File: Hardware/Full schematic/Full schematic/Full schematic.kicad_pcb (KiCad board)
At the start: 2 copper layers, 111 parts, among them J1 Conn_01x04_Male, J2 Conn_01x04_Male, J3 Conn_01x02_Male, J4 Conn_01x02_Male, J5 Conn_01x02_Male, J6 Conn_01x02_Male, J7 Conn_01x02_Male, J8 Conn_01x06_Male, K1 EDR101A0500, K2 EDR101A0500, K3 EDR101A0500, K4 EDR101A0500, K5 EDR101A0500, Q1 BSS138, Q2 IRF610, Q3 IRLML2502, Q4 IRLML2502, Q5 IRLML2502, Q6 IRLML2502, Q7 IRLML2502, U1 74LVC2T45DC, U2 74LVC2T45DC, U3 AD9835, X1 50MHz

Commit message: After prototype built
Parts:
- C23: value 0.01uF -> 10nF
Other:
- board outline added: 83.6 x 61.5 mm

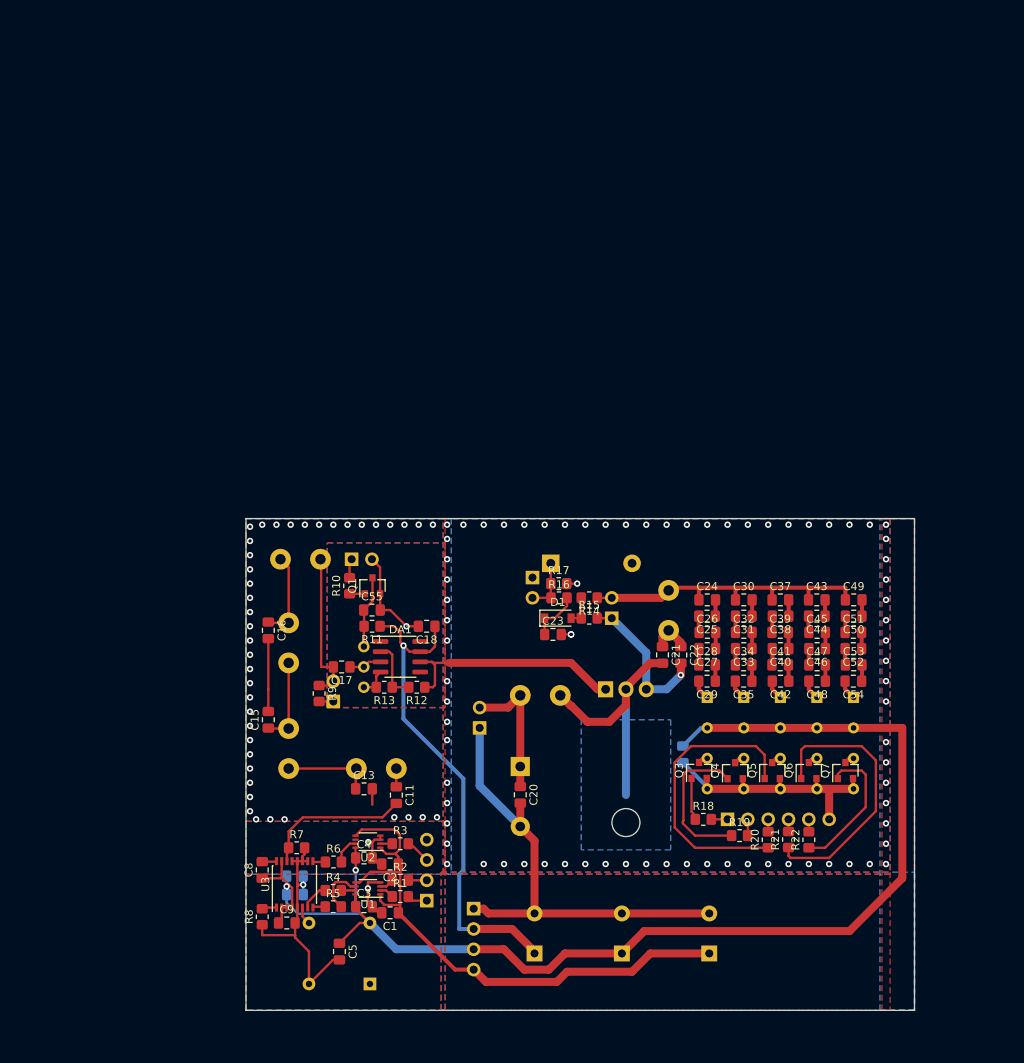
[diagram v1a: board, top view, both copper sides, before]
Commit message: Second prototype PCB is almost ready
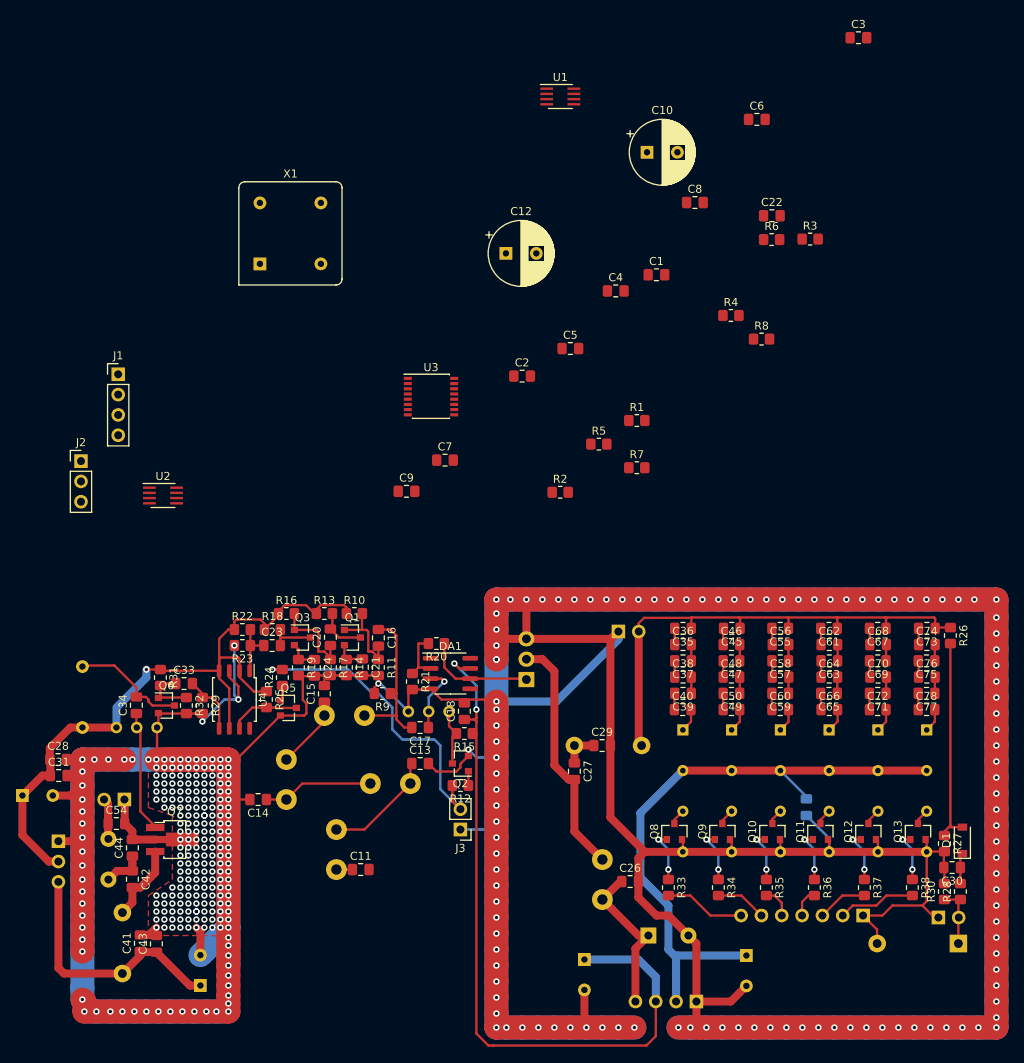
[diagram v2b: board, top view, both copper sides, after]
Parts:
- added C56: 100pF, Capacitor_SMD:C_0805_2012Metric_Pad1.18x1.45mm_HandSolder, F.Cu at (142.8, 103.6)
- added C57: 100pF, Capacitor_SMD:C_0805_2012Metric_Pad1.18x1.45mm_HandSolder, F.Cu at (142.7, 105.7)
- added C58: 100pF, Capacitor_SMD:C_0805_2012Metric_Pad1.18x1.45mm_HandSolder, F.Cu at (142.8, 107.7)
- added C59: 100pF, Capacitor_SMD:C_0805_2012Metric_Pad1.18x1.45mm_HandSolder, F.Cu at (142.7, 109.7)
- added C60: 100pF, Capacitor_SMD:C_0805_2012Metric_Pad1.18x1.45mm_HandSolder, F.Cu at (142.7, 111.8)
- added C61: 47pF, Capacitor_SMD:C_0805_2012Metric_Pad1.18x1.45mm_HandSolder, F.Cu at (148.8, 101.6)
- added C62: 47pF, Capacitor_SMD:C_0805_2012Metric_Pad1.18x1.45mm_HandSolder, F.Cu at (148.9, 103.6)
- added C63: 47pF, Capacitor_SMD:C_0805_2012Metric_Pad1.18x1.45mm_HandSolder, F.Cu at (148.9, 105.7)
- added C64: 47pF, Capacitor_SMD:C_0805_2012Metric_Pad1.18x1.45mm_HandSolder, F.Cu at (148.9, 107.7)
- added C65: 47pF, Capacitor_SMD:C_0805_2012Metric_Pad1.18x1.45mm_HandSolder, F.Cu at (148.8, 109.7)
- added C66: 47pF, Capacitor_SMD:C_0805_2012Metric_Pad1.18x1.45mm_HandSolder, F.Cu at (148.9, 111.8)
- added C67: 24pF, Capacitor_SMD:C_0805_2012Metric_Pad1.18x1.45mm_HandSolder, F.Cu at (154.9, 101.6)
- added C68: 24pF, Capacitor_SMD:C_0805_2012Metric_Pad1.18x1.45mm_HandSolder, F.Cu at (155.0, 103.6)
- added C69: 24pF, Capacitor_SMD:C_0805_2012Metric_Pad1.18x1.45mm_HandSolder, F.Cu at (154.9, 105.7)
- added C70: 24pF, Capacitor_SMD:C_0805_2012Metric_Pad1.18x1.45mm_HandSolder, F.Cu at (155.0, 107.7)
- added C71: 24pF, Capacitor_SMD:C_0805_2012Metric_Pad1.18x1.45mm_HandSolder, F.Cu at (154.9, 109.7)
- added C72: 24pF, Capacitor_SMD:C_0805_2012Metric_Pad1.18x1.45mm_HandSolder, F.Cu at (154.9, 111.8)
- added C73: 12pF, Capacitor_SMD:C_0805_2012Metric_Pad1.18x1.45mm_HandSolder, F.Cu at (161.1, 101.6)
- added C74: 12pF, Capacitor_SMD:C_0805_2012Metric_Pad1.18x1.45mm_HandSolder, F.Cu at (161.1, 103.6)
- added C75: 12pF, Capacitor_SMD:C_0805_2012Metric_Pad1.18x1.45mm_HandSolder, F.Cu at (161.0, 105.7)
- added C76: 12pF, Capacitor_SMD:C_0805_2012Metric_Pad1.18x1.45mm_HandSolder, F.Cu at (161.1, 107.7)
- added C77: 12pF, Capacitor_SMD:C_0805_2012Metric_Pad1.18x1.45mm_HandSolder, F.Cu at (161.0, 109.7)
- added C78: 12pF, Capacitor_SMD:C_0805_2012Metric_Pad1.18x1.45mm_HandSolder, F.Cu at (161.0, 111.8)
- added J9: Conn_01x07_Male, Connector_PinHeader_2.54mm:PinHeader_1x07_P2.54mm_Vertical, B.Cu at (153.1, 137.5)
- added K6: EDR101A0500, Relay_THT:Relay_SPST_StandexMeder_SIL_Form1A, B.Cu at (161.0, 114.3)
- added L7: 200nH, Inductor_THT:L_Axial_L5.3mm_D2.2mm_P7.62mm_Horizontal_Vishay_IM-1, B.Cu at (55.5, 114.0)
- added L8: 300nH, Inductor_THT:L_Axial_L16.0mm_D7.5mm_P7.62mm_Vertical_Fastron_XHBCC, B.Cu at (60.5, 144.8)
- added L9: 23.5nH, Inductor_THT:L_Axial_L9.5mm_D4.0mm_P5.08mm_Vertical_Fastron_SMCC, B.Cu at (58.8, 133.0)
- added Q10: IRLML2502, Package_TO_SOT_SMD:SOT-23, F.Cu at (141.8, 127.0)
- added Q11: IRLML2502, Package_TO_SOT_SMD:SOT-23, F.Cu at (147.8, 127.0)
- added Q12: IRLML2502, Package_TO_SOT_SMD:SOT-23, F.Cu at (153.8, 127.0)
- added Q13: IRLML2502, Package_TO_SOT_SMD:SOT-23, F.Cu at (159.9, 127.0)
- added Q8: IRLML2502, Package_TO_SOT_SMD:SOT-23, F.Cu at (129.5, 127.0)
- added Q9: IRLML2502, Package_TO_SOT_SMD:SOT-23, F.Cu at (135.5, 127.0)
- added R23: 4.7k, Resistor_SMD:R_0805_2012Metric_Pad1.20x1.40mm_HandSolder, F.Cu at (75.5, 103.8)
- added R24: 100, Resistor_SMD:R_0805_2012Metric_Pad1.20x1.40mm_HandSolder, F.Cu at (80.5, 107.8)
- added R25: 47k, Resistor_SMD:R_0805_2012Metric_Pad1.20x1.40mm_HandSolder, F.Cu at (78.5, 110.5)
- added R26: 220k, Resistor_SMD:R_0805_2012Metric_Pad1.20x1.40mm_HandSolder, F.Cu at (164.0, 102.5)
- added R27: 11k, Resistor_SMD:R_0805_2012Metric_Pad1.20x1.40mm_HandSolder, F.Cu at (163.2, 128.5)
- added R28: 39k, Resistor_SMD:R_0805_2012Metric_Pad1.20x1.40mm_HandSolder, F.Cu at (165.2, 134.5)
- added R29: 33, Resistor_SMD:R_0805_2012Metric_Pad1.20x1.40mm_HandSolder, F.Cu at (70.5, 111.2)
- added R30: 10k, Resistor_SMD:R_0805_2012Metric_Pad1.20x1.40mm_HandSolder, F.Cu at (163.2, 134.5)
- added R31: 6.2k, Resistor_SMD:R_0805_2012Metric_Pad1.20x1.40mm_HandSolder, F.Cu at (65.2, 107.8)
- added R32: 1k, Resistor_SMD:R_0805_2012Metric_Pad1.20x1.40mm_HandSolder, F.Cu at (68.5, 111.2)
- added R33: 100, Resistor_SMD:R_0805_2012Metric_Pad1.20x1.40mm_HandSolder, F.Cu at (128.8, 134.0)
- added R34: 100, Resistor_SMD:R_0805_2012Metric_Pad1.20x1.40mm_HandSolder, F.Cu at (135.0, 134.0)
- added R35: 100, Resistor_SMD:R_0805_2012Metric_Pad1.20x1.40mm_HandSolder, F.Cu at (141.0, 134.0)
- added R36: 100, Resistor_SMD:R_0805_2012Metric_Pad1.20x1.40mm_HandSolder, F.Cu at (147.0, 134.0)
- added R37: 100, Resistor_SMD:R_0805_2012Metric_Pad1.20x1.40mm_HandSolder, F.Cu at (153.2, 134.0)
- added R38: 100, Resistor_SMD:R_0805_2012Metric_Pad1.20x1.40mm_HandSolder, F.Cu at (159.2, 134.0)
- added RV2: 20k, Potentiometer_THT:Potentiometer_Bourns_3386C_Horizontal, B.Cu at (59.8, 114.0)
- added U4: ICS501, Package_SO:SOIC-8_5.23x5.23mm_P1.27mm, F.Cu at (74.5, 110.5)
- C10, C12: footprint Capacitor_THT:CP_Radial_D10.0mm_P5.00mm -> Capacitor_THT:CP_Radial_D8.0mm_P3.80mm; moved to F.Cu
- C14: value 470uF x 16V -> 56pF; footprint Capacitor_THT:CP_Radial_D10.0mm_P5.00mm -> Capacitor_SMD:C_0805_2012Metric_Pad1.18x1.45mm_HandSolder; moved to F.Cu
- C15: value 56pF -> 47pF
- C16, C43: value 47pF -> 0.1uF
- C19: value 1000uF x 25V -> 470uFx16V; footprint Capacitor_THT:CP_Radial_D14.0mm_P7.50mm -> Capacitor_THT:CP_Radial_D8.0mm_P3.80mm
- C22: value 75pF -> 10nF
- C23: value 10nF -> 0.1uF
- C24, C26, C27: value 390pF -> 0.1uF
- C25: value 390pF -> 1000uF x 25V; footprint Capacitor_SMD:C_0805_2012Metric_Pad1.18x1.45mm_HandSolder -> Capacitor_THT:CP_Radial_D10.0mm_P5.00mm; moved to B.Cu
- C28: value 390pF -> 1nF
- C29: value 390pF -> 75pF
- C30: value 200pF -> 10nF
- C31: value 200pF -> 0.1uF
- C32: value 200pF -> 470uFx6.3V; footprint Capacitor_SMD:C_0805_2012Metric_Pad1.18x1.45mm_HandSolder -> Capacitor_THT:CP_Radial_D8.0mm_P3.80mm; moved to B.Cu
- C33: value 200pF -> 1nF
- C34: value 200pF -> 75pF
- C35: value 200pF -> 390pF
- C36: value 0.1uF -> 390pF; moved to F.Cu
- C37, C38, C39, C40: value 100pF -> 390pF
- C41, C42: value 100pF -> 1nF
- C44: value 47pF -> 20pF
- C45, C46, C47, C48: value 47pF -> 200pF
- C49, C50: value 24pF -> 200pF
- C51: value 24pF -> 470uF x 10V; footprint Capacitor_SMD:C_0805_2012Metric_Pad1.18x1.45mm_HandSolder -> Capacitor_THT:CP_Radial_D8.0mm_P3.80mm; moved to B.Cu
- C52: value 24pF -> 470uFx6.3V; footprint Capacitor_SMD:C_0805_2012Metric_Pad1.18x1.45mm_HandSolder -> Capacitor_THT:CP_Radial_D8.0mm_P3.80mm; moved to B.Cu
- C53: value 24pF -> 0.1uF; moved to B.Cu
- C54: value 24pF -> 56pF
- C55: value 10nF -> 100pF
- C6, C7, J1, J3, X1: moved to F.Cu
- J2: value Conn_01x04_Male -> Conn_01x03_Male; footprint Connector_PinHeader_2.54mm:PinHeader_1x04_P2.54mm_Vertical -> Connector_PinHeader_2.54mm:PinHeader_1x03_P2.54mm_Vertical; moved to F.Cu
- J4: value Conn_01x02_Male -> Conn_01x04_Male; footprint Connector_PinHeader_2.54mm:PinHeader_1x02_P2.54mm_Vertical -> Connector_PinHeader_2.54mm:PinHeader_1x04_P2.54mm_Vertical
- J5: value Conn_01x02_Male -> Conn_01x03_Male; footprint Connector_PinHeader_2.54mm:PinHeader_1x02_P2.54mm_Vertical -> Connector_PinHeader_2.54mm:PinHeader_1x03_P2.54mm_Vertical
- J8: value Conn_01x06_Male -> Conn_01x02_Male; footprint Connector_PinHeader_2.54mm:PinHeader_1x06_P2.54mm_Vertical -> Connector_PinHeader_2.54mm:PinHeader_1x02_P2.54mm_Vertical
- K1, K2, K3, K4, K5: footprint Relay_THT:Relay_SPST_StandexMeder_MS_Form1AB -> Relay_THT:Relay_SPST_StandexMeder_SIL_Form1A
- L6: footprint Inductor_THT:L_Radial_D9.5mm_P5.00mm_Fastron_07HVP -> Inductor_THT:L_Toroid_Vertical_L21.6mm_W9.1mm_P8.40mm_Bourns_5700
- Q1: value BSS138 -> BC847
- Q2: value IRF610 -> BSS138; footprint Package_TO_SOT_THT:TO-220-3_Horizontal_TabDown -> Package_TO_SOT_SMD:SOT-23; moved to F.Cu
- Q3: value IRLML2502 -> BC847
- Q4: value IRLML2502 -> IRF610; footprint Package_TO_SOT_SMD:SOT-23 -> Package_TO_SOT_THT:TO-220-3_Vertical; moved to B.Cu
- Q5: value IRLML2502 -> BSS138
- Q6: value IRLML2502 -> BFS17
- Q7: value IRLML2502 -> AFT05MS003N; footprint Package_TO_SOT_SMD:SOT-23 -> Package_TO_SOT_SMD:SOT-89-3_Handsoldering
- R10: value 100 -> 30k
- R11: value 56k -> 6.8k
- R12: value 3.9k -> 100
- R13: value 2k -> 1k
- R14: value 220k -> 100
- R15: value 11k -> 56k
- R16: value 39k -> 30k
- R17: value 10k -> 6.8k
- R18: value 100 -> 1k
- R20: value 100 -> 3.9k
- R21: value 100 -> 2k
- R22: value 100 -> 4.7k
- U1, U2: footprint Package_SO:VSSOP-8_2.3x2mm_P0.5mm -> Package_SO:SSOP-8_2.95x2.8mm_P0.65mm
- moved C3 125.0 mm to (152.5, 27.8)
- moved C6 112.8 mm to (139.8, 38.0)
- moved U1 101.9 mm to (115.2, 35.1), turned to 0 degrees
- moved C10 100.4 mm to (126.1, 42.1), turned to 0 degrees
- moved C8 99.4 mm to (132.1, 48.4), turned to 0 degrees
- moved R8 95.4 mm to (140.4, 65.4), turned to 0 degrees
- moved R6 95.2 mm to (141.7, 53.0)
- moved C54 93.8 mm to (59.8, 126.0), turned to 0 degrees
- moved C43 93.1 mm to (64.8, 141.0), turned to 90 degrees
- moved C51 92.8 mm to (70.2, 146.2), turned to 90 degrees
- moved C32 92.5 mm to (48.0, 122.5)
- moved R3 91.3 mm to (146.5, 52.9)
- moved X1 91.0 mm to (77.7, 56.0), turned to 0 degrees
- moved C44 90.3 mm to (61.8, 129.0), turned to 90 degrees
- moved C12 88.7 mm to (108.4, 54.7), turned to 0 degrees
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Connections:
- C1 pad 1: +3V3 -> PWR_CMN_3.3
- C10 pad 1: +3V3 -> PWR_CMN_3.3
- C12 pad 1: +5V -> PWR_CMN_5
- C14 pad 1: +12V -> Net-(C14-Pad1)
- C16 pad 2: GND -> Net-(C16-Pad2)
- C17 pad 2: Net-(C17-Pad2) -> Net-(C16-Pad1)
- C18 pad 1: +12V -> PWR_3.5_12
- C19 pad 1: Net-(C19-Pad1) -> PWR_3.5_12
- C2 pad 1: +3V3 -> PWR_CMN_3.3
- C20 pad 1: Net-(C19-Pad1) -> Net-(C20-Pad1)
- C20 pad 2: GND -> Net-(C20-Pad2)
- C21 pad 2: Net-(C21-Pad2) -> GND
- C22 pad 1: Net-(C21-Pad1) -> Net-(C22-Pad1)
- C23 pad 2: GND -> Net-(C23-Pad2)
- C24 pad 1: ANT_3.5 -> Net-(C24-Pad1)
- C24 pad 2: Net-(C24-Pad2) -> GND
- C25 pad 1: Net-(C24-Pad2) -> PWR_3.5_OUT
- C25 pad 2: Net-(C25-Pad2) -> GND
- C26 pad 1: Net-(C25-Pad2) -> PWR_3.5_OUT
- C26 pad 2: Net-(C26-Pad2) -> GND
- C27 pad 1: Net-(C26-Pad2) -> Net-(C27-Pad1)
- C28 pad 1: Net-(C27-Pad2) -> PWR_144_5
- C28 pad 2: Net-(C28-Pad2) -> GND
- C29 pad 1: Net-(C28-Pad2) -> Net-(C27-Pad1)
- C29 pad 2: Net-(C29-Pad2) -> GND
- C3 pad 1: +5V -> PWR_CMN_5
- C30 pad 1: ANT_3.5 -> Net-(C30-Pad1)
- C30 pad 2: Net-(C30-Pad2) -> GND
- C31 pad 1: Net-(C30-Pad2) -> PWR_144_5
- C31 pad 2: Net-(C31-Pad2) -> GND
- C32 pad 1: Net-(C31-Pad2) -> PWR_144_5
- C32 pad 2: Net-(C32-Pad2) -> GND
- C33 pad 1: Net-(C32-Pad2) -> Net-(C33-Pad1)
- C34 pad 1: Net-(C33-Pad2) -> Net-(C34-Pad1)
- C35 pad 1: Net-(C34-Pad2) -> ANT_3.5
- C36 pad 1: +5V -> Net-(C35-Pad2)
- C36 pad 2: GND -> Net-(C36-Pad2)
- C37 pad 1: ANT_3.5 -> Net-(C36-Pad2)
- C4 pad 1: +5V -> PWR_CMN_5
- C41 pad 1: Net-(C40-Pad2) -> PWR_144_OUT
- C41 pad 2: Net-(C41-Pad2) -> GND
- C42 pad 1: Net-(C41-Pad2) -> Net-(C42-Pad1)
- C43 pad 1: ANT_3.5 -> PWR_144_OUT
- C43 pad 2: Net-(C43-Pad2) -> GND
- C44 pad 1: Net-(C43-Pad2) -> Net-(C42-Pad1)
- C44 pad 2: Net-(C44-Pad2) -> GND
- C45 pad 1: Net-(C44-Pad2) -> ANT_3.5
- C49 pad 1: ANT_3.5 -> Net-(C48-Pad2)
- C5 pad 1: +5V -> PWR_CMN_5
- C51 pad 1: Net-(C50-Pad2) -> PWR_144_OUT
- C51 pad 2: Net-(C51-Pad2) -> GND
- C52 pad 1: Net-(C51-Pad2) -> PWR_3.5_5
- C52 pad 2: Net-(C52-Pad2) -> GND
- C53 pad 1: Net-(C52-Pad2) -> PWR_3.5_5
- C53 pad 2: Net-(C53-Pad2) -> GND
- C54 pad 1: Net-(C53-Pad2) -> Net-(C54-Pad1)
- C54 pad 2: Net-(C54-Pad2) -> GND
- C55 pad 1: Net-(C55-Pad1) -> ANT_3.5
- C55 pad 2: GND -> Net-(C55-Pad2)
- C6 pad 1: +5V -> PWR_CMN_5
- C7 pad 1: +5V -> PWR_CMN_5
- C8 pad 1: +5V -> PWR_CMN_5
- D1 pad 1: Net-(C23-Pad1) -> Net-(C30-Pad1)
- DA1 pad 7: +12V -> PWR_3.5_12
- J1 pad 1: Net-(J1-Pad1) -> GND
- J1 pad 4: GND -> Net-(J1-Pad4)
- J2 pad 2: +12V -> PWR_CMN_3.3
- J2 pad 3: +5V -> PWR_CMN_5
- J3 pad 2: Net-(C17-Pad2) -> Manipulation
- J4 pad 1: Net-(J4-Pad1) -> GND
- J4 pad 2: GND -> PWR_3.5_5
- J5 pad 2: Net-(C19-Pad1) -> PWR_144_5
- J8 pad 1: Net-(J8-Pad1) -> GND
- J8 pad 2: Net-(J8-Pad2) -> Net-(C54-Pad1)
- K1 pad 1: Net-(C29-Pad2) -> Net-(C40-Pad2)
- K1 pad 3: +5V -> PWR_3.5_5
- K2 pad 1: Net-(C35-Pad2) -> Net-(C50-Pad2)
- K2 pad 3: +5V -> PWR_3.5_5
- K3 pad 1: Net-(C42-Pad2) -> Net-(C60-Pad2)
- K3 pad 3: +5V -> PWR_3.5_5
- K4 pad 1: Net-(C48-Pad2) -> Net-(C66-Pad2)
- K4 pad 3: +5V -> PWR_3.5_5
- K5 pad 1: Net-(C54-Pad2) -> Net-(C72-Pad2)
- K5 pad 3: +5V -> PWR_3.5_5
- L2 pad 2: Net-(C15-Pad1) -> Net-(C14-Pad1)
- L3 pad 1: Net-(C15-Pad1) -> Net-(C14-Pad1)
- L3 pad 2: Net-(C16-Pad1) -> Net-(C15-Pad1)
- L4 pad 1: Net-(C16-Pad1) -> Net-(C15-Pad1)
- L4 pad 2: Net-(C17-Pad2) -> Net-(C16-Pad1)
- L5 pad 1: Net-(C19-Pad1) -> PWR_3.5_OUT
- L5 pad 2: Net-(C21-Pad2) -> Net-(C27-Pad2)
- L6 pad 1: Net-(C21-Pad1) -> Net-(C27-Pad1)
- Q1 pad 1: Net-(Q1-Pad1) -> Net-(C16-Pad2)
- Q1 pad 2: GND -> Net-(C21-Pad1)
- Q1 pad 3: Net-(C55-Pad1) -> Net-(C20-Pad2)
- Q2 pad 1: Net-(DA1-Pad6) -> Net-(Q2-Pad1)
- Q2 pad 2: Net-(C21-Pad2) -> GND
- Q2 pad 3: GND -> Net-(C22-Pad1)
- Q3 pad 1: Net-(Q3-Pad1) -> Net-(C20-Pad1)
- Q3 pad 2: GND -> Net-(C24-Pad1)
- Q3 pad 3: Net-(K1-Pad5) -> Net-(C23-Pad2)
- Q4 pad 1: Net-(Q4-Pad1) -> Net-(DA1-Pad6)
- Q4 pad 2: GND -> Net-(C27-Pad2)
- Q4 pad 3: Net-(K2-Pad5) -> GND
- Q5 pad 3: Net-(K3-Pad5) -> Net-(Q5-Pad3)
- Q6 pad 1: Net-(Q6-Pad1) -> Net-(C33-Pad1)
- Q6 pad 3: Net-(K4-Pad5) -> Net-(C34-Pad2)
- Q7 pad 1: Net-(Q7-Pad1) -> Net-(C34-Pad1)
- Q7 pad 3: Net-(K5-Pad5) -> Net-(C42-Pad2)
- R1 pad 2: Net-(J1-Pad1) -> Net-(J1-Pad4)
- R10 pad 1: Net-(Q1-Pad1) -> PWR_144_5
- R10 pad 2: Net-(J4-Pad1) -> Net-(C16-Pad2)
- R11 pad 1: +12V -> Net-(C16-Pad2)
- R11 pad 2: Net-(C55-Pad1) -> GND
- R12 pad 1: Net-(DA1-Pad6) -> Net-(Q2-Pad1)
- R12 pad 2: Net-(DA1-Pad2) -> Manipulation
- R13 pad 1: Net-(DA1-Pad2) -> PWR_144_5
- R13 pad 2: GND -> Net-(C20-Pad2)
- R14 pad 1: ANT_3.5 -> Net-(C21-Pad1)
- R14 pad 2: Net-(D1-Pad2) -> GND
- R15 pad 1: Net-(D1-Pad2) -> PWR_3.5_12
- R15 pad 2: GND -> Net-(C22-Pad1)
- R16 pad 1: Net-(D2-Pad1) -> PWR_144_5
- R16 pad 2: Net-(C23-Pad1) -> Net-(C20-Pad1)
- R17 pad 1: Net-(D2-Pad1) -> Net-(C20-Pad1)
- R18 pad 1: Net-(Q3-Pad1) -> PWR_144_5
- R18 pad 2: Net-(J8-Pad1) -> Net-(C23-Pad2)
- R19 pad 1: Net-(Q4-Pad1) -> Net-(C24-Pad1)
- R19 pad 2: Net-(J8-Pad2) -> GND
- R2 pad 2: Net-(J1-Pad2) -> Net-(J1-Pad3)
- R20 pad 1: Net-(Q5-Pad1) -> Net-(DA1-Pad6)
- R20 pad 2: Net-(J8-Pad3) -> Net-(DA1-Pad2)
- R21 pad 1: Net-(Q6-Pad1) -> Net-(DA1-Pad2)
- R21 pad 2: Net-(J8-Pad4) -> GND
- R22 pad 1: Net-(Q7-Pad1) -> PWR_144_5
- R22 pad 2: Net-(J8-Pad5) -> Net-(C23-Pad1)
- R3 pad 2: Net-(J1-Pad3) -> Net-(J1-Pad2)
- R9 pad 1: Net-(C17-Pad2) -> Net-(C16-Pad1)
- RV1 pad 3: Net-(C55-Pad1) -> Net-(C22-Pad1)
- U1 pad 1: +3V3 -> PWR_CMN_3.3
- U1 pad 5: +3V3 -> PWR_CMN_3.3
- U1 pad 6: Net-(R5-Pad2) -> Net-(R4-Pad2)
- U1 pad 7: Net-(R4-Pad2) -> Net-(R6-Pad2)
- U1 pad 8: +5V -> PWR_CMN_5
- U2 pad 1: +3V3 -> PWR_CMN_3.3
- U2 pad 5: +3V3 -> PWR_CMN_3.3
- U2 pad 7: Net-(R6-Pad2) -> Net-(R5-Pad2)
- U2 pad 8: +5V -> PWR_CMN_5
- U3 pad 15: +5V -> PWR_CMN_5
- U3 pad 4: +5V -> PWR_CMN_5
- U3 pad 7: Net-(R4-Pad1) -> Net-(R6-Pad1)
- U3 pad 8: Net-(R5-Pad1) -> Net-(R4-Pad1)
- U3 pad 9: Net-(R6-Pad1) -> Net-(R5-Pad1)
- X1 pad 8: +5V -> PWR_CMN_5
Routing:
- net GND: track 187.4 -> 954.8 mm, vias 123 -> 355
- net +5V: track 162.5 -> 0.00 mm, vias 2 -> 0
- net PWR_3.5_12: track 0.00 -> 92.8 mm, vias 0 -> 2
- net PWR_144_5: track 0.00 -> 89.5 mm, vias 0 -> 1
- net PWR_3.5_5: track 0.00 -> 77.2 mm
- net +3V3: track 72.5 -> 0.00 mm
- net +12V: track 61.3 -> 0.00 mm, vias 1 -> 0
- net Manipulation: track 0.00 -> 40.2 mm, vias 0 -> 1
- net Net-(Q6-Pad1): track 34.7 -> 0.00 mm
- net Net-(Q5-Pad1): track 36.4 -> 1.95 mm
- net PWR_144_OUT: track 0.00 -> 32.0 mm
- net Net-(C21-Pad2): track 31.7 -> 0.00 mm
- net Net-(C27-Pad2): track 2.04 -> 30.6 mm
- net ANT_3.5: track 39.2 -> 62.9 mm
- net Net-(D1-Pad2): track 3.81 -> 26.0 mm
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- removed copper zone on B.Cu, net GND
- removed copper zone on B.Cu, net Net-(C21-Pad2)
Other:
- board outline removed

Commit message: Second prototype PCB seems to be ready
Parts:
- C1, C10, C12, C2, C3, C4, C6, C7, J1, J2, J3, X1: moved to B.Cu
- moved C3 132.3 mm to (90.4, 144.6)
- moved C6 117.3 mm to (80.6, 139.2)
- moved U1 109.9 mm to (90.4, 142.2), turned to 180 degrees
- moved C10 108.1 mm to (101.6, 147.4), turned to 270 degrees
- moved R6 106.5 mm to (84.4, 142.8)
- moved C8 103.0 mm to (76.6, 135.2), turned to 90 degrees
- moved R8 98.0 mm to (76.6, 139.8), turned to 90 degrees
- moved R3 97.9 mm to (95.2, 136.4)
- moved C12 96.8 mm to (91.0, 150.0)
- moved R4 93.5 mm to (85.4, 140.8)
- moved C1 90.6 mm to (90.4, 140.2)
- moved X1 89.8 mm to (78.2, 145.8)
- moved C5 89.6 mm to (82.4, 149.4), turned to 90 degrees
- moved J2 89.4 mm to (104.2, 155.6), turned to 90 degrees
- moved C4 84.6 mm to (90.4, 137.9)
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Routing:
- net GND: track 954.8 -> 1048.6 mm, vias 355 -> 433
- net PWR_CMN_5: track 0.00 -> 73.9 mm, vias 0 -> 5
- net PWR_CMN_3.3: track 0.00 -> 56.3 mm, vias 0 -> 2
- net Net-(U3-Pad6): track 0.00 -> 17.9 mm
- net Net-(C11-Pad2): track 0.00 -> 6.61 mm
- net Net-(R6-Pad2): track 0.00 -> 3.41 mm
- net Net-(R8-Pad2): track 0.00 -> 3.31 mm
- net Net-(J1-Pad2): track 0.00 -> 2.99 mm
- net Net-(J1-Pad3): track 0.00 -> 2.78 mm
- net Net-(R4-Pad2): track 0.00 -> 2.75 mm
- net Net-(C9-Pad1): track 0.00 -> 2.73 mm
- net Net-(R6-Pad1): track 0.00 -> 2.71 mm
- net Net-(R5-Pad2): track 0.00 -> 2.66 mm
- net Net-(J1-Pad4): track 0.00 -> 2.56 mm
- net Net-(C8-Pad2): track 0.00 -> 2.38 mm
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- added copper zone on B.Cu, net GND
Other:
- board outline added: 128 x 62.4 mm

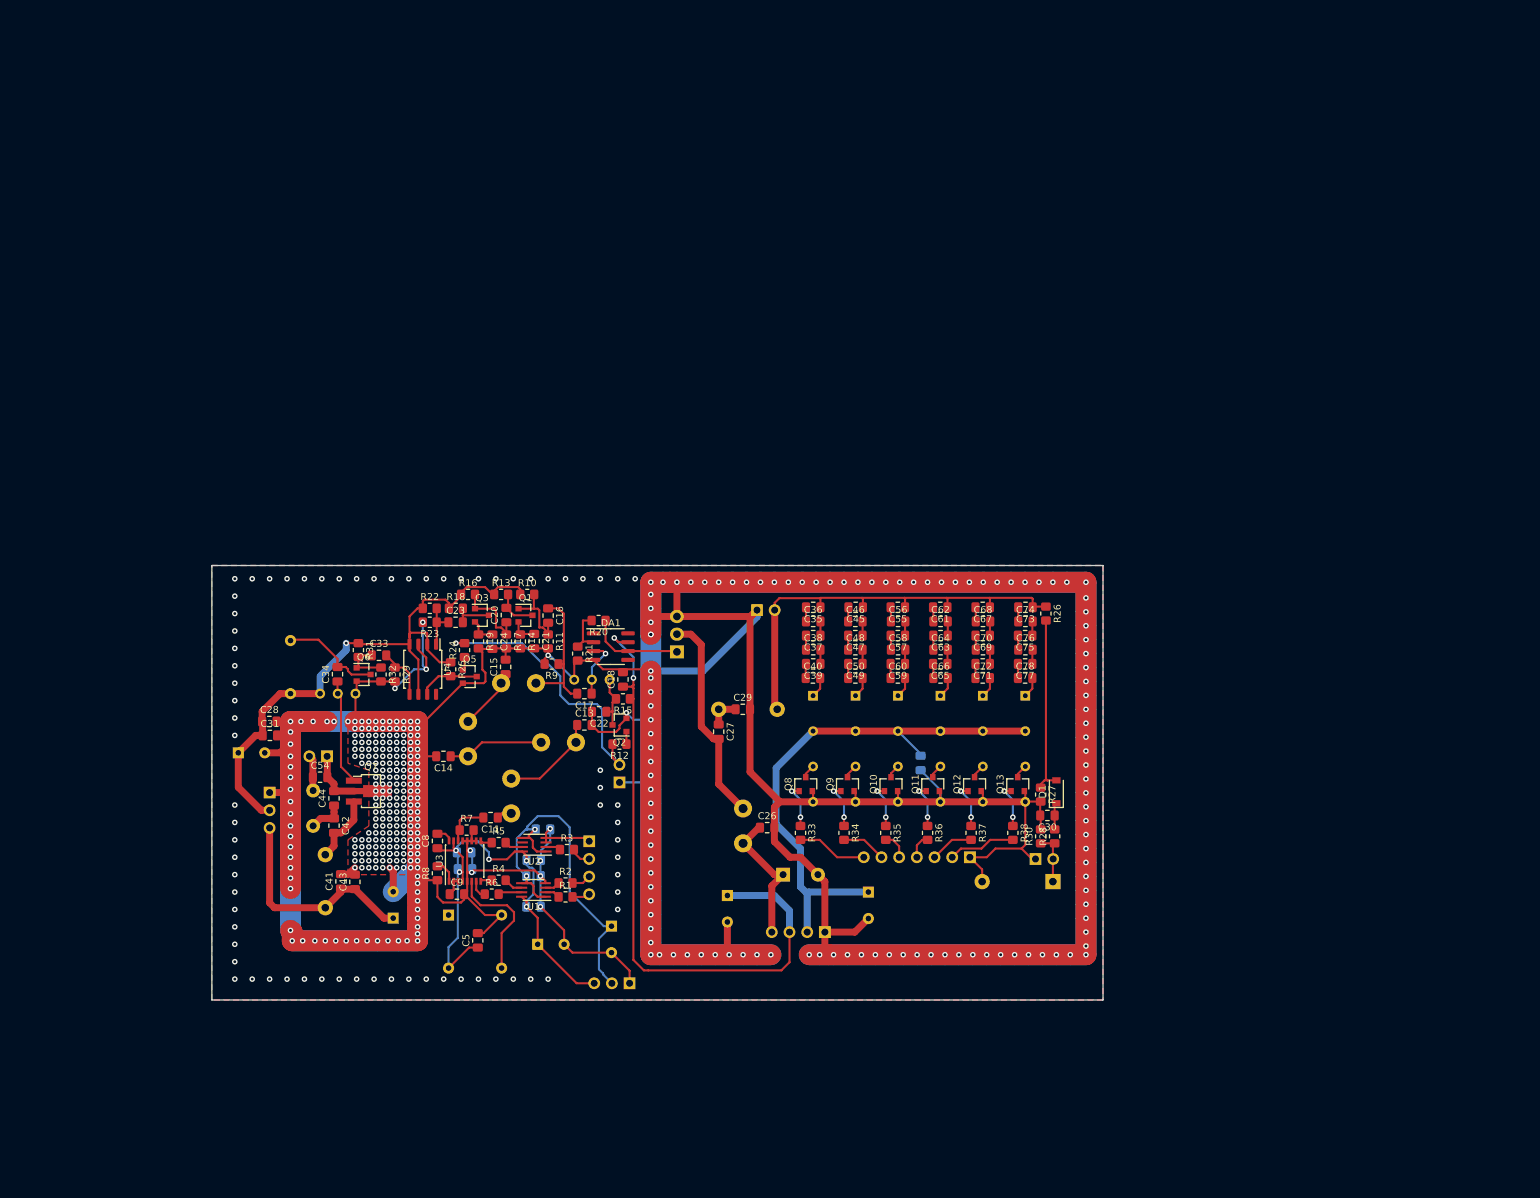
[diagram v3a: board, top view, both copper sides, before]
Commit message: 144MHz part is ready except antenna
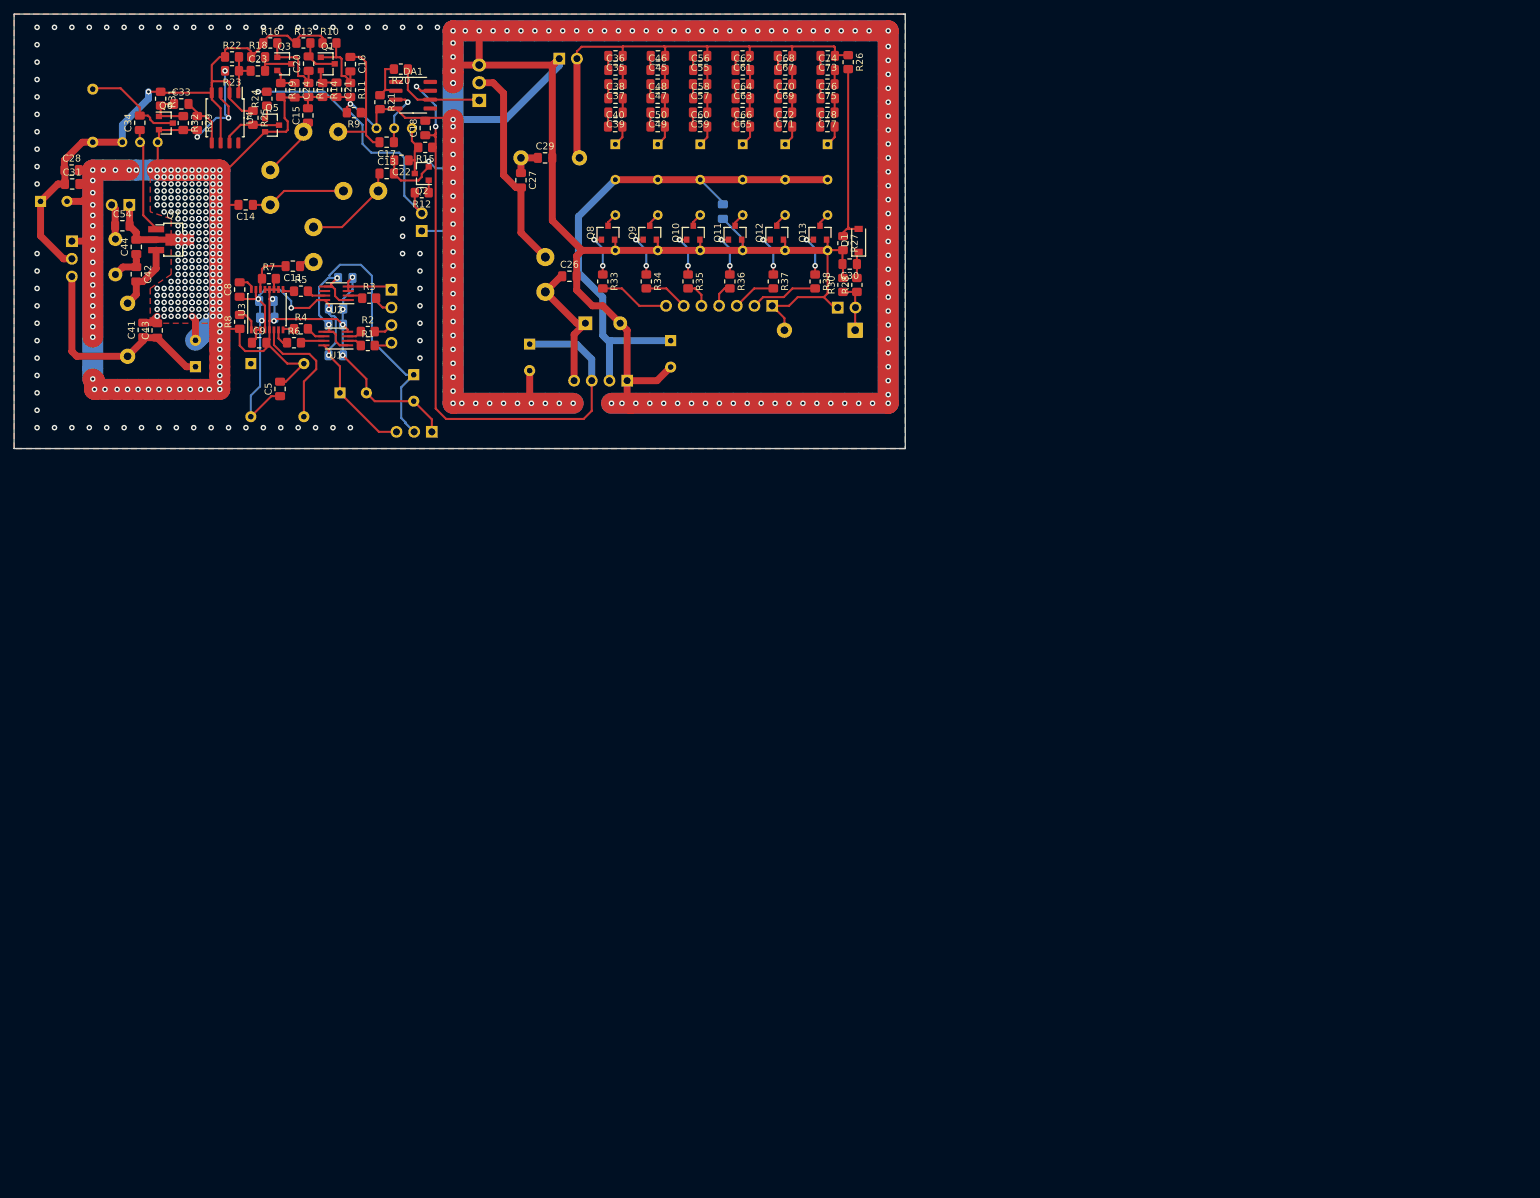
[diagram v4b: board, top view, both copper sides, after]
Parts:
- moved C11 84.1 mm to (55.8, 52.6)
- moved C7 84.1 mm to (52.0, 57.6)
- moved C9 84.1 mm to (51.0, 63.6)
- moved J5 84.1 mm to (24.1, 49.0)
- moved R4 84.1 mm to (57.0, 61.6)
- moved R6 84.1 mm to (56.0, 63.6)
- moved U3 84.1 mm to (52.1, 58.9)
- moved X1 84.1 mm to (49.8, 66.6)
- moved C12 84.1 mm to (62.6, 70.8)
- moved C13 84.1 mm to (69.3, 39.3)
- moved C14 84.1 mm to (49.1, 43.8)
- moved C17 84.1 mm to (69.3, 34.8)
- moved C18 84.1 mm to (74.8, 32.8)
- moved C19 84.1 mm to (89.8, 63.8)
- moved C2 84.1 mm to (63.4, 54.3)
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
